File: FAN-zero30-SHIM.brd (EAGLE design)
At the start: 38.3 x 65 mm, 10 parts

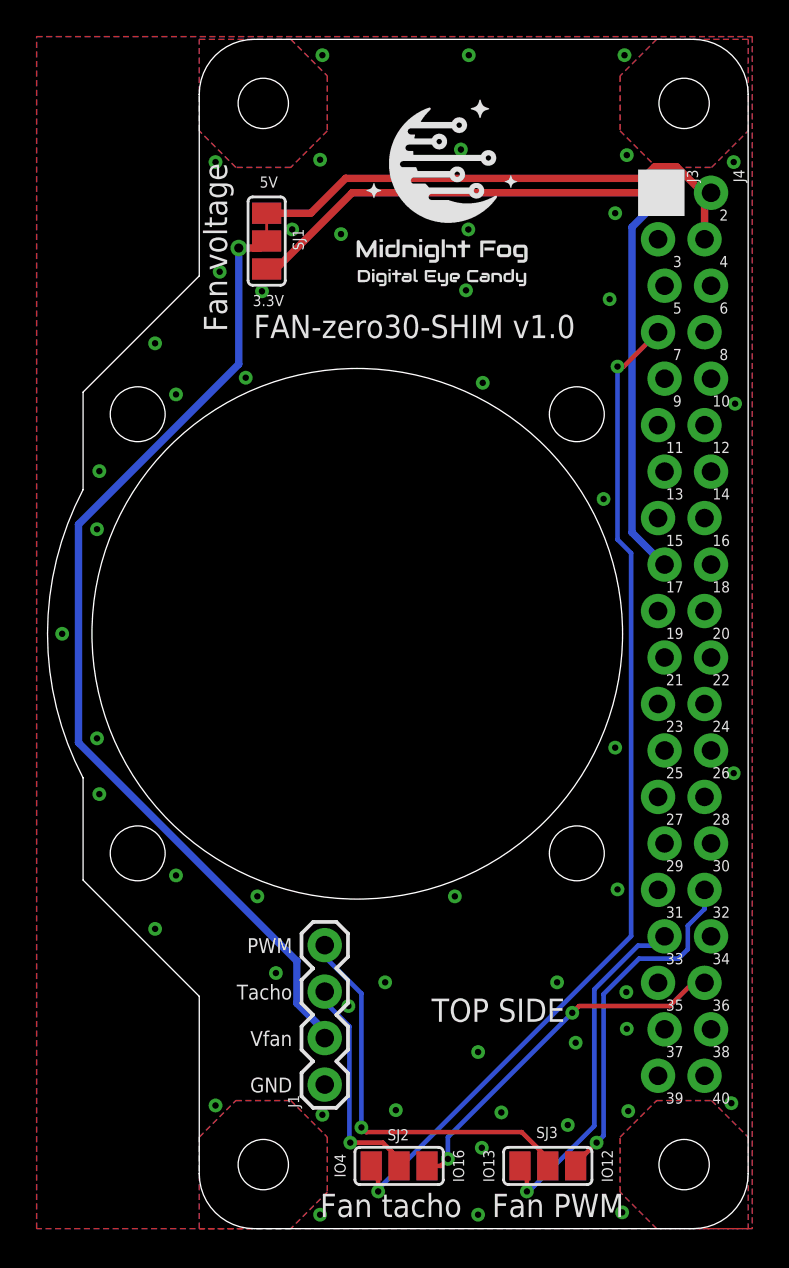
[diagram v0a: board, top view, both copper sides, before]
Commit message: - Fixed VFAN trace on zero30 board. - Generated new CAM. - Generated new PNG preview image.
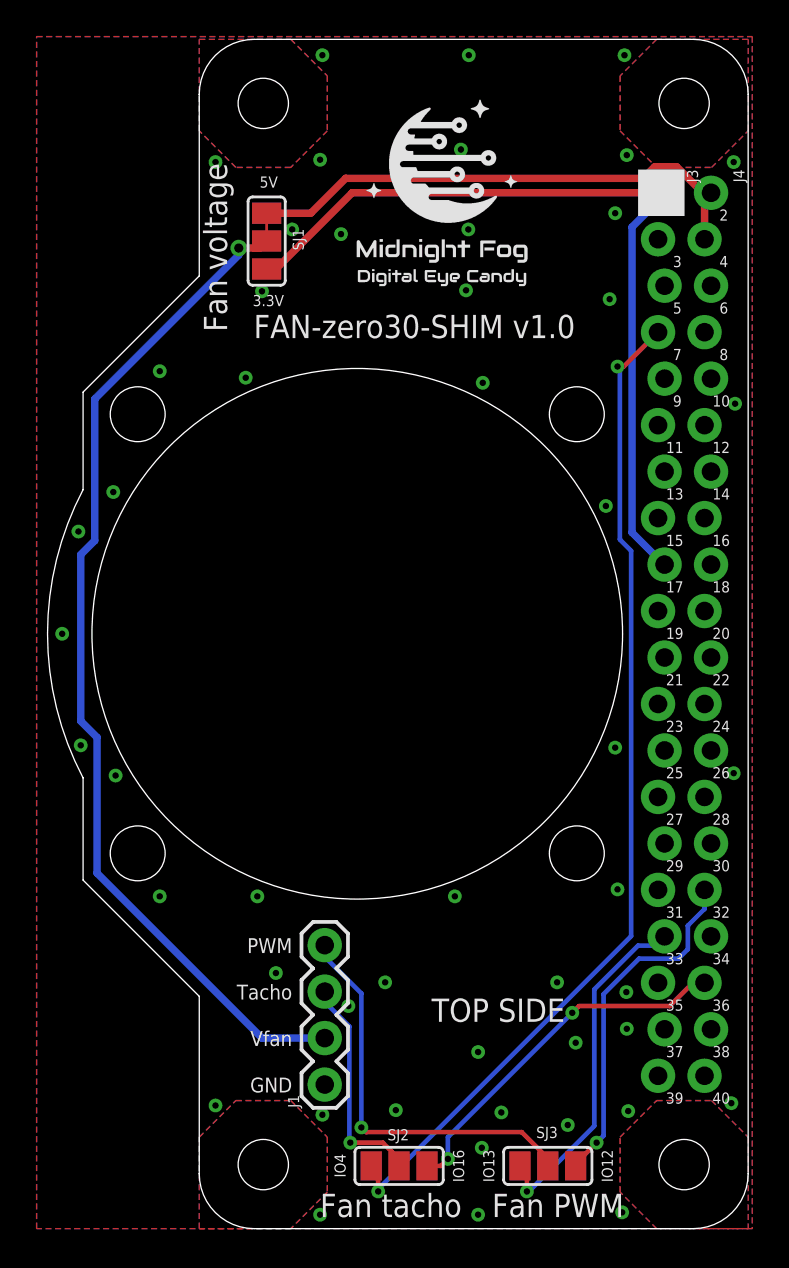
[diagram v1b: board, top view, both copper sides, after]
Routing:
- net VFAN: track 55.2 -> 57.1 mm
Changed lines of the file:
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@@
 <via x="22.86" y="18.542" extent="1-16" drill="0.35"/>
 <via x="19.558" y="13.462" extent="1-16" drill="0.35"/>
-<via x="-5.588" y="26.797" extent="1-16" drill="0.35"/>
 <via x="-7.493" y="32.512" extent="1-16" drill="0.35"/>
-<via x="-5.588" y="38.227" extent="1-16" drill="0.35"/>
-<via x="-5.461" y="23.749" extent="1-16" drill="0.35"/>
-<via x="-1.27" y="19.304" extent="1-16" drill="0.35"/>
-<via x="-2.413" y="16.383" extent="1-16" drill="0.35"/>
+<via x="-2.159" y="18.161" extent="1-16" drill="0.35"/>
 <via x="4.191" y="13.97" extent="1-16" drill="0.35"/>
-<via x="-5.461" y="41.402" extent="1-16" drill="0.35"/>
-<via x="-1.27" y="45.593" extent="1-16" drill="0.35"/>
-<via x="-2.413" y="48.387" extent="1-16" drill="0.35"/>
+<via x="-2.159" y="46.863" extent="1-16" drill="0.35"/>
 <via x="0.889" y="58.293" extent="1-16" drill="0.35"/>
 <via x="6.731" y="64.135" extent="1-16" drill="0.35"/>
@@
 <via x="6.604" y="58.42" extent="1-16" drill="0.35"/>
 <via x="7.747" y="54.356" extent="1-16" drill="0.35"/>
-<via x="22.098" y="39.878" extent="1-16" drill="0.35"/>
+<via x="22.225" y="39.497" extent="1-16" drill="0.35"/>
 <via x="15.494" y="46.228" extent="1-16" drill="0.35"/>
 <via x="2.54" y="46.5074" extent="1-16" drill="0.35"/>
@@
 <via x="14.5796" y="51.2826" extent="1-16" drill="0.35"/>
 <via x="3.429" y="51.2318" extent="1-16" drill="0.35"/>
-<via x="1.1176" y="52.2986" extent="1-16" drill="0.35"/>
 <via x="20.1422" y="5.6642" extent="1-16" drill="0.35"/>
 <via x="23.4442" y="6.4262" extent="1-16" drill="0.35"/>
+<via x="-4.699" y="40.259" extent="1-16" drill="0.35"/>
+<via x="-6.604" y="38.1" extent="1-16" drill="0.35"/>
+<via x="-6.477" y="26.416" extent="1-16" drill="0.35"/>
+<via x="-4.572" y="24.765" extent="1-16" drill="0.35"/>
 </signal>
 <signal name="3.3V">
@@
 <wire x1="23.1982" y1="47.117" x2="22.86" y2="47.117" width="0.254" layer="1"/>
 <via x="22.86" y="47.117" extent="1-16" drill="0.35"/>
-<wire x1="22.86" y1="47.117" x2="22.86" y2="37.66523125" width="0.254" layer="16"/>
-<wire x1="22.86" y1="37.66523125" x2="23.603" y2="36.92223125" width="0.254" layer="16"/>
+<wire x1="22.86" y1="47.117" x2="22.987" y2="46.99" width="0.254" layer="16"/>
+<wire x1="22.987" y1="46.99" x2="22.987" y2="37.66523125" width="0.254" layer="16"/>
+<wire x1="22.987" y1="37.66523125" x2="23.603" y2="37.04923125" width="0.254" layer="16"/>
 <via x="9.779" y="2.032" extent="1-16" drill="0.35"/>
-<wire x1="23.603" y1="36.92223125" x2="23.603" y2="15.983" width="0.254" layer="16"/>
+<wire x1="23.603" y1="37.04923125" x2="23.603" y2="15.983" width="0.254" layer="16"/>
 <wire x1="23.603" y1="15.983" x2="9.779" y2="2.159" width="0.254" layer="16"/>
 <wire x1="9.779" y1="2.159" x2="9.779" y2="2.032" width="0.254" layer="16"/>
@@
 <wire x1="3.302" y1="53.594" x2="2.159" y2="53.594" width="0.4064" layer="1"/>
 <via x="2.159" y="53.594" extent="1-16" drill="0.5"/>
-<wire x1="6.858" y1="10.795" x2="6.858" y2="10.414" width="0.4064" layer="16"/>
-<wire x1="6.858" y1="10.795" x2="5.334" y2="12.319" width="0.4064" layer="16"/>
-<wire x1="2.159" y1="53.594" x2="2.159" y2="47.24719375" width="0.4064" layer="16"/>
-<wire x1="2.159" y1="47.24719375" x2="-6.6006" y2="38.48759375" width="0.4064" layer="16"/>
-<wire x1="-6.6006" y1="38.48759375" x2="-6.6006" y2="26.56180625" width="0.4064" layer="16"/>
-<wire x1="-6.6006" y1="26.56180625" x2="5.334" y2="14.62720625" width="0.4064" layer="16"/>
-<wire x1="5.334" y1="14.62720625" x2="5.334" y2="12.319" width="0.4064" layer="16"/>
+<wire x1="2.159" y1="53.594" x2="2.159" y2="53.213" width="0.4064" layer="16"/>
+<wire x1="2.159" y1="53.213" x2="-5.71269375" y2="45.34130625" width="0.4064" layer="16"/>
+<wire x1="-5.71269375" y1="37.59940625" x2="-5.71269375" y2="45.34130625" width="0.4064" layer="16"/>
+<wire x1="3.429" y1="10.414" x2="6.858" y2="10.414" width="0.4064" layer="16"/>
+<wire x1="3.429" y1="10.414" x2="-5.58569375" y2="19.42869375" width="0.4064" layer="16"/>
+<wire x1="-6.477" y1="36.8351" x2="-5.71269375" y2="37.59940625" width="0.4064" layer="16"/>
+<wire x1="-6.477" y1="27.744234375" x2="-6.477" y2="36.8351" width="0.4064" layer="16"/>
+<wire x1="-5.58569375" y1="26.852928125" x2="-6.477" y2="27.744234375" width="0.4064" layer="16"/>
+<wire x1="-5.58569375" y1="19.42869375" x2="-5.58569375" y2="26.852928125" width="0.4064" layer="16"/>
 </signal>
 <signal name="TACH">
